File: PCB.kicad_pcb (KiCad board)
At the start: 4 copper layers, 43 parts, among them J1 USB_C_Receptacle_USB2.0, J2 JST - 1.00mm 4 Pin, SW1 MX_SW_solder, SW2 MX_SW_solder, SW3 MX_SW_solder, SW4 MX_SW_solder, SW72 SW_Push, SW73 SW_Push, U1 RP2040, U3 USBLC6-2SC6, U4 3.3V Fixed Regulator, U5 ZD25D40CNJGR, Y1 12MHz Crystal 3225

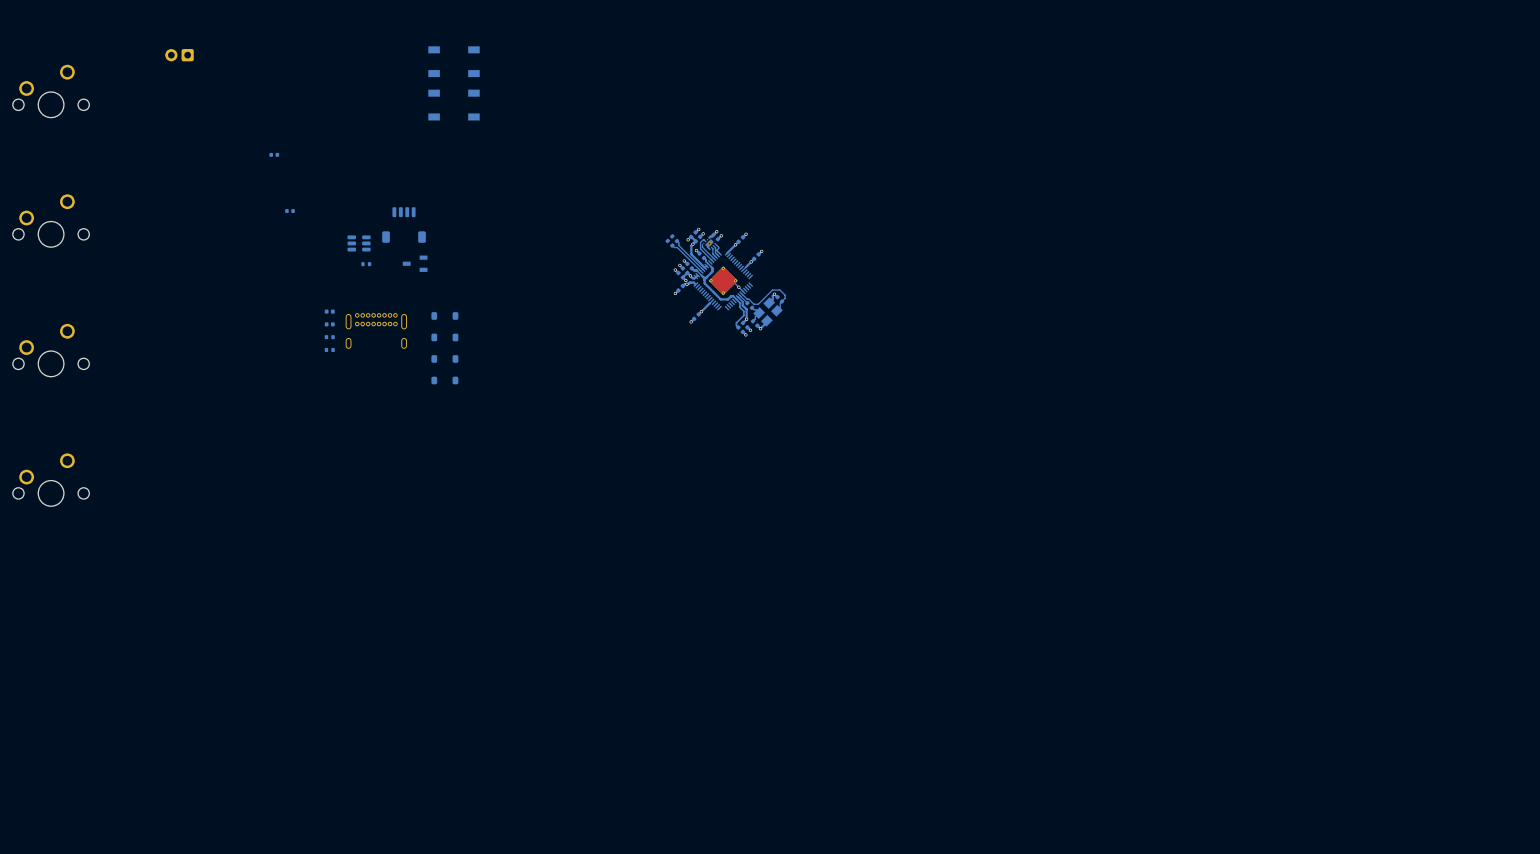
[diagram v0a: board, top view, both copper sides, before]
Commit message: Update Schematic with keyboard layout
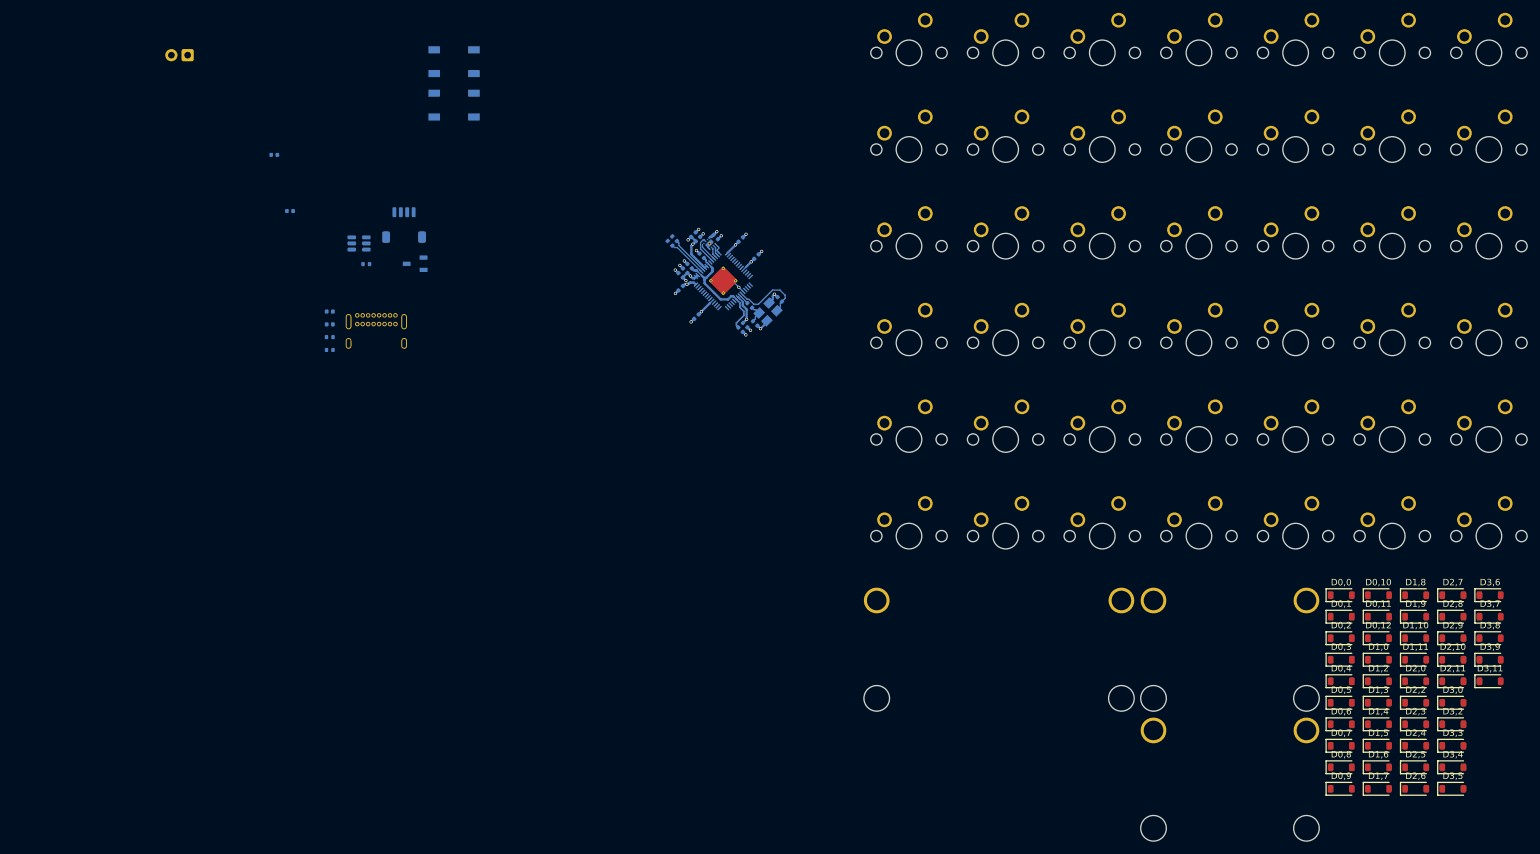
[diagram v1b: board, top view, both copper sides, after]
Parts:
- removed D1, D2, D3, D4: D_Small, Diode_SMD:D_SOD-123
- removed SW1, SW2, SW3, SW4: MX_SW_solder, marbastlib-mx:SW_MX_1u
- added D0,0: 1N4148W, Diode_SMD:D_SOD-123, F.Cu at (245.0, 115.7)
- added D0,1: 1N4148W, Diode_SMD:D_SOD-123, F.Cu at (245.0, 119.0)
- added D0,10: 1N4148W, Diode_SMD:D_SOD-123, F.Cu at (250.8, 115.7)
- added D0,11: 1N4148W, Diode_SMD:D_SOD-123, F.Cu at (250.8, 119.0)
- added D0,12: 1N4148W, Diode_SMD:D_SOD-123, F.Cu at (250.8, 122.4)
- added D0,2: 1N4148W, Diode_SMD:D_SOD-123, F.Cu at (245.0, 122.4)
- added D0,3: 1N4148W, Diode_SMD:D_SOD-123, F.Cu at (245.0, 125.7)
- added D0,4: 1N4148W, Diode_SMD:D_SOD-123, F.Cu at (245.0, 129.1)
- added D0,5: 1N4148W, Diode_SMD:D_SOD-123, F.Cu at (245.0, 132.4)
- added D0,6: 1N4148W, Diode_SMD:D_SOD-123, F.Cu at (245.0, 135.8)
- added D0,7: 1N4148W, Diode_SMD:D_SOD-123, F.Cu at (245.0, 139.1)
- added D0,8: 1N4148W, Diode_SMD:D_SOD-123, F.Cu at (245.0, 142.5)
- added D0,9: 1N4148W, Diode_SMD:D_SOD-123, F.Cu at (245.0, 145.8)
- added D1,0: 1N4148W, Diode_SMD:D_SOD-123, F.Cu at (250.8, 125.7)
- added D1,10: 1N4148W, Diode_SMD:D_SOD-123, F.Cu at (256.6, 122.4)
- added D1,11: 1N4148W, Diode_SMD:D_SOD-123, F.Cu at (256.6, 125.7)
- added D1,2: 1N4148W, Diode_SMD:D_SOD-123, F.Cu at (250.8, 129.1)
- added D1,3: 1N4148W, Diode_SMD:D_SOD-123, F.Cu at (250.8, 132.4)
- added D1,4: 1N4148W, Diode_SMD:D_SOD-123, F.Cu at (250.8, 135.8)
- added D1,5: 1N4148W, Diode_SMD:D_SOD-123, F.Cu at (250.8, 139.1)
- added D1,6: 1N4148W, Diode_SMD:D_SOD-123, F.Cu at (250.8, 142.5)
- added D1,7: 1N4148W, Diode_SMD:D_SOD-123, F.Cu at (250.8, 145.8)
- added D1,8: 1N4148W, Diode_SMD:D_SOD-123, F.Cu at (256.6, 115.7)
- added D1,9: 1N4148W, Diode_SMD:D_SOD-123, F.Cu at (256.6, 119.0)
- added D2,0: 1N4148W, Diode_SMD:D_SOD-123, F.Cu at (256.6, 129.1)
- added D2,10: 1N4148W, Diode_SMD:D_SOD-123, F.Cu at (262.4, 125.7)
- added D2,11: 1N4148W, Diode_SMD:D_SOD-123, F.Cu at (262.4, 129.1)
- added D2,2: 1N4148W, Diode_SMD:D_SOD-123, F.Cu at (256.6, 132.4)
- added D2,3: 1N4148W, Diode_SMD:D_SOD-123, F.Cu at (256.6, 135.8)
- added D2,4: 1N4148W, Diode_SMD:D_SOD-123, F.Cu at (256.6, 139.1)
- added D2,5: 1N4148W, Diode_SMD:D_SOD-123, F.Cu at (256.6, 142.5)
- added D2,6: 1N4148W, Diode_SMD:D_SOD-123, F.Cu at (256.6, 145.8)
- added D2,7: 1N4148W, Diode_SMD:D_SOD-123, F.Cu at (262.4, 115.7)
- added D2,8: 1N4148W, Diode_SMD:D_SOD-123, F.Cu at (262.4, 119.0)
- added D2,9: 1N4148W, Diode_SMD:D_SOD-123, F.Cu at (262.4, 122.4)
- added D3,0: 1N4148W, Diode_SMD:D_SOD-123, F.Cu at (262.4, 132.4)
- added D3,11: 1N4148W, Diode_SMD:D_SOD-123, F.Cu at (268.2, 129.1)
- added D3,2: 1N4148W, Diode_SMD:D_SOD-123, F.Cu at (262.4, 135.8)
- added D3,3: 1N4148W, Diode_SMD:D_SOD-123, F.Cu at (262.4, 139.1)
- added D3,4: 1N4148W, Diode_SMD:D_SOD-123, F.Cu at (262.4, 142.5)
- added D3,5: 1N4148W, Diode_SMD:D_SOD-123, F.Cu at (262.4, 145.8)
- added D3,6: 1N4148W, Diode_SMD:D_SOD-123, F.Cu at (268.2, 115.7)
- added D3,7: 1N4148W, Diode_SMD:D_SOD-123, F.Cu at (268.2, 119.0)
- added D3,8: 1N4148W, Diode_SMD:D_SOD-123, F.Cu at (268.2, 122.4)
- added D3,9: 1N4148W, Diode_SMD:D_SOD-123, F.Cu at (268.2, 125.7)
- added SW0,0: MX_SW_solder, PCM_marbastlib-mx:SW_MX_1u, F.Cu at (177.7, 31.2)
- added SW0,1: MX_SW_solder, PCM_marbastlib-mx:SW_MX_1u, F.Cu at (177.7, 46.3)
- added SW0,10: MX_SW_solder, PCM_marbastlib-mx:SW_MX_1u, F.Cu at (192.7, 91.4)
- added SW0,11: MX_SW_solder, PCM_marbastlib-mx:SW_MX_1u, F.Cu at (192.7, 106.5)
- added SW0,12: MX_SW_solder, PCM_marbastlib-mx:SW_MX_1.5u, F.Cu at (207.8, 31.2)
- added SW0,2: MX_SW_solder, PCM_marbastlib-mx:SW_MX_1u, F.Cu at (177.7, 61.3)
- added SW0,3: MX_SW_solder, PCM_marbastlib-mx:SW_MX_1u, F.Cu at (177.7, 76.4)
- added SW0,4: MX_SW_solder, PCM_marbastlib-mx:SW_MX_1u, F.Cu at (177.7, 91.4)
- added SW0,5: MX_SW_solder, PCM_marbastlib-mx:SW_MX_1u, F.Cu at (177.7, 106.5)
- added SW0,6: MX_SW_solder, PCM_marbastlib-mx:SW_MX_1u, F.Cu at (192.7, 31.2)
- added SW0,7: MX_SW_solder, PCM_marbastlib-mx:SW_MX_1u, F.Cu at (192.7, 46.3)
- added SW0,8: MX_SW_solder, PCM_marbastlib-mx:SW_MX_1u, F.Cu at (192.7, 61.3)
- added SW0,9: MX_SW_solder, PCM_marbastlib-mx:SW_MX_1u, F.Cu at (192.7, 76.4)
- added SW1,0: MX_SW_solder, PCM_marbastlib-mx:SW_MX_1.75u, F.Cu at (207.8, 46.3)
- added SW1,10: MX_SW_solder, PCM_marbastlib-mx:SW_MX_1u, F.Cu at (222.8, 91.4)
- added SW1,11: MX_SW_solder, PCM_marbastlib-mx:STAB_MX_P_2.25u, F.Cu at (227.7, 123.5)
- added SW1,2: MX_SW_solder, PCM_marbastlib-mx:SW_MX_1u, F.Cu at (207.8, 61.3)
- added SW1,3: MX_SW_solder, PCM_marbastlib-mx:SW_MX_1u, F.Cu at (207.8, 76.4)
- added SW1,4: MX_SW_solder, PCM_marbastlib-mx:SW_MX_1u, F.Cu at (207.8, 91.4)
- added SW1,5: MX_SW_solder, PCM_marbastlib-mx:SW_MX_1u, F.Cu at (207.8, 106.5)
- added SW1,6: MX_SW_solder, PCM_marbastlib-mx:SW_MX_1u, F.Cu at (222.8, 31.2)
- added SW1,7: MX_SW_solder, PCM_marbastlib-mx:SW_MX_1u, F.Cu at (222.8, 46.3)
- added SW1,8: MX_SW_solder, PCM_marbastlib-mx:SW_MX_1u, F.Cu at (222.8, 61.3)
- added SW1,9: MX_SW_solder, PCM_marbastlib-mx:SW_MX_1u, F.Cu at (222.8, 76.4)
- added SW2,0: MX_SW_solder, PCM_marbastlib-mx:SW_MX_1.5u, F.Cu at (222.8, 106.5)
- added SW2,10: MX_SW_solder, PCM_marbastlib-mx:SW_MX_1u, F.Cu at (252.9, 61.3)
- added SW2,11: MX_SW_solder, PCM_marbastlib-mx:STAB_MX_P_2u, F.Cu at (227.7, 143.7)
- added SW2,2: MX_SW_solder, PCM_marbastlib-mx:SW_MX_1u, F.Cu at (237.9, 31.2)
- added SW2,3: MX_SW_solder, PCM_marbastlib-mx:SW_MX_1u, F.Cu at (237.9, 46.3)
- added SW2,4: MX_SW_solder, PCM_marbastlib-mx:SW_MX_1u, F.Cu at (237.9, 61.3)
- added SW2,5: MX_SW_solder, PCM_marbastlib-mx:SW_MX_1u, F.Cu at (237.9, 76.4)
- added SW2,6: MX_SW_solder, PCM_marbastlib-mx:SW_MX_1u, F.Cu at (237.9, 91.4)
- added SW2,7: MX_SW_solder, PCM_marbastlib-mx:SW_MX_1u, F.Cu at (237.9, 106.5)
- added SW2,8: MX_SW_solder, PCM_marbastlib-mx:SW_MX_1u, F.Cu at (252.9, 31.2)
- added SW2,9: MX_SW_solder, PCM_marbastlib-mx:SW_MX_1u, F.Cu at (252.9, 46.3)
- added SW3,0: MX_SW_solder, PCM_marbastlib-mx:SW_MX_1u, F.Cu at (252.9, 76.4)
- added SW3,11: MX_SW_solder, PCM_marbastlib-mx:SW_MX_1u, F.Cu at (268.0, 106.5)
- added SW3,2: MX_SW_solder, PCM_marbastlib-mx:SW_MX_1u, F.Cu at (252.9, 91.4)
- added SW3,3: MX_SW_solder, PCM_marbastlib-mx:SW_MX_1u, F.Cu at (252.9, 106.5)
- added SW3,4: MX_SW_solder, PCM_marbastlib-mx:SW_MX_1.25u, F.Cu at (268.0, 31.2)
- added SW3,5: MX_SW_solder, PCM_marbastlib-mx:STAB_MX_P_3u, F.Cu at (191.7, 123.5)
- added SW3,6: MX_SW_solder, PCM_marbastlib-mx:SW_MX_1u, F.Cu at (268.0, 46.3)
- added SW3,7: MX_SW_solder, PCM_marbastlib-mx:SW_MX_1.25u, F.Cu at (268.0, 61.3)
- added SW3,8: MX_SW_solder, PCM_marbastlib-mx:SW_MX_1.25u, F.Cu at (268.0, 76.4)
- added SW3,9: MX_SW_solder, PCM_marbastlib-mx:SW_MX_1.25u, F.Cu at (268.0, 91.4)
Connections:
- U1 pad 11: GP8 -> Col8
- U1 pad 12: GP9 -> Col9
- U1 pad 13: GP10 -> Col10
- U1 pad 14: GP11 -> Col11
- U1 pad 15: GP12 -> Col12
- U1 pad 2: GP0 -> Col0
- U1 pad 3: GP1 -> Col1
- U1 pad 4: GP2 -> Col2
- U1 pad 5: GP3 -> Col3
- U1 pad 6: GP4 -> Col4
- U1 pad 7: GP5 -> Col5
- U1 pad 8: GP6 -> Col6
- U1 pad 9: GP7 -> Col7

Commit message: First pcb footprints
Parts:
- moved SW0,0 144.0 mm to (33.7, 33.3)
- moved SW0,1 136.2 mm to (41.9, 57.1)
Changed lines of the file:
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@@
 	(footprint "PCM_marbastlib-mx:SW_MX_1u"
 		(layer "F.Cu")
-		(at 177.67 31.24)
+		(at 33.655 33.3375)
 		(descr "Footprint for Cherry MX style switches")
 		(tags "cherry mx switch")
@@
 	(footprint "PCM_marbastlib-mx:SW_MX_1u"
 		(layer "F.Cu")
-		(at 177.67 46.29)
+		(at 41.91 57.15)
 		(descr "Footprint for Cherry MX style switches")
 		(tags "cherry mx switch")
